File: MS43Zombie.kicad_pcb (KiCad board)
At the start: 2 copper layers, 165 x 119.2 mm, 223 parts, among them IC1 XL1509-5.0E1, IC10 NCV8402ASTT1G, IC11 NCV8402ASTT1G, IC12 TJA1020T_CM,118, IC13 NCV8402ASTT1G, IC14 NCV8402ASTT1G, IC15 NCV8402ASTT1G, IC16 NCV8402ASTT1G, IC17 TJA1055T_3_C,518, IC18 MCP25625T-E_ML, IC19 NCV7356D1R2G, IC2 M24M02-DRMN6TP, IC20 MAX3221ECPWR, IC21 FAN3122TMX, IC22 FAN3122TMX, IC23 FAN3122TMX, IC24 AD5160BRJZ5-R2, IC25 AD5160BRJZ5-R2, IC26 TDA2822D013TR, IC3 NCV8402ASTT1G, IC4 NCV8402ASTT1G, IC5 NCV8402ASTT1G, IC6 NCV8402ASTT1G, IC7 NCV8402ASTT1G, IC8 NCV7356D1R2G, IC9 NUP1105LT1G, J1 7-967288-1, J3 75867-101LF, J4 Conn_01x03, Q1 MMBT3904, Q2 NCV8461DR2G, Q3 MMBT3904, Q4 MMBT3904, Q5 MMBT3904, U1 AMS1117-3.3, U12 SN65HVD230, U16 SN65HVD230, U17 STM32F107VCT6, U19 SN65HVD230, U3 SN65HVD230, U4 SN65HVD230, U8 SN65HVD230, Y1 X50328MSB2GI, Y2 X322516MLB4SI

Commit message: Checkpoint before trying 4 layer
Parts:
- removed C1, C71: 470uF 25V, Capacitor_SMD:CP_Elec_10x10
- removed C11, C2, C37, C38, C39, C40, C41, C5, C52, C57, C70, C73: 0.1uF, Capacitor_SMD:C_0805_2012Metric
- removed C16, C47, C48: 100pF, Capacitor_SMD:C_0805_2012Metric
- removed C18, C20, C22, C26, C42, C43, C49, C51, C59, C60, C61, C7, C72, C76, C77: 1uF, Capacitor_SMD:C_0805_2012Metric
- removed C3: 10uF, Capacitor_SMD:C_0805_2012Metric
- removed C35, C36: 22pF, Capacitor_SMD:C_0805_2012Metric
- removed C45: 10nF, Capacitor_SMD:C_0805_2012Metric
- removed C53, C55, C56: 0.47uF, Capacitor_SMD:C_0805_2012Metric
- removed C6, C8, C9: 100uF 6.3V, Capacitor_Tantalum_SMD:CP_EIA-1608-08_AVX-J
- removed C74, C75: 100uF, Capacitor_Tantalum_SMD:CP_EIA-1608-08_AVX-J
- removed D1, D2: SS54B, SamacSys_Parts:DIOM5336X244N
- removed D10, D12: 1N4148W-7-F, digikey-footprints:SOD-123
- removed D3, D6: LED, LED_SMD:LED_0805_2012Metric
- removed D8: 12V, Diode_SMD:D_SOD-123
- removed FB2: MH2029-300Y, SamacSys_Parts:BEADC2016X130N
- removed IC10, IC11, IC13, IC15, IC16, IC5: NCV8402ASTT1G, SamacSys_Parts:SOT230P700X175-4N
- removed IC17: TJA1055T_3_C,518, SamacSys_Parts:SOIC127P600X175-14N
- removed IC18: MCP25625T-E_ML, SamacSys_Parts:QFN65P600X600X100-29N-D
- removed IC19, IC8: NCV7356D1R2G, SamacSys_Parts:SOIC127P600X175-8N
- removed IC20: MAX3221ECPWR, SamacSys_Parts:SOP65P640X120-16N
- removed IC21, IC22, IC23: FAN3122TMX, SamacSys_Parts:SOIC127P600X175-8N
- removed IC26: TDA2822D013TR, SamacSys_Parts:SOIC127P600X175-8N
- removed IC9: NUP1105LT1G, SamacSys_Parts:SOT96P237X111-3N
- removed JP1, JP10, JP11, JP12, JP13, JP14, JP15, JP2, JP3, JP4, JP5, JP6, JP7, JP8, JP9: SolderJumper_2_Open, Jumper:SolderJumper-2_P1.3mm_Open_Pad1.0x1.5mm
- removed L1: SWRB1207S-680MT, SamacSys_Parts:INDPM125125X800N
- removed R13: 2.7K, Resistor_SMD:R_0805_2012Metric
- removed R14: 6.49k, Resistor_SMD:R_0805_2012Metric
- removed R15: 1k, Resistor_SMD:R_0805_2012Metric
- removed R18, R29: 4K7, Resistor_SMD:R_0805_2012Metric
- removed R19, R30: 1K5, Resistor_SMD:R_0805_2012Metric
- removed R45, R46, R57, R58, R59, R62, R63, R71, R73: 1K, Resistor_SMD:R_0805_2012Metric
- removed R55, R61: 2K7, Resistor_SMD:R_0805_2012Metric
- removed R65: 120R, Resistor_SMD:R_0805_2012Metric
- removed R66, R67: 4R7, Resistor_SMD:R_0805_2012Metric
- removed R69, R70: 10K, Resistor_SMD:R_0805_2012Metric
- removed U1: AMS1117-3.3, Package_TO_SOT_SMD:SOT-223-3_TabPin2
- removed U17: STM32F107VCT6, Package_QFP:LQFP-100_14x14mm_P0.5mm
- removed Y1: X50328MSB2GI, SamacSys_Parts:RESC5032X135N
- removed Y2: X322516MLB4SI, SamacSys_Parts:X322516MLB4SI
- added IC27: NCV8402ASTT1G, SamacSys_Parts:SOT230P700X175-4N, F.Cu at (117.4, 65.2)
- added J2: EXT1, Connector_PinHeader_2.54mm:PinHeader_2x20_P2.54mm_Vertical, B.Cu at (164.4, 131.3)
- added Q6: NCV8461DR2G, SamacSys_Parts:SOIC127P600X175-8N, F.Cu at (211.4, 65.2)
- added Q7: MMBT3904, Package_TO_SOT_SMD:SOT-23, F.Cu at (203.8, 75.4)
- C4: value 0.1uF -> 1uF
- IC1: value XL1509-5.0E1 -> NCV8402ASTT1G; footprint SamacSys_Parts:SOIC127P600X175-8N -> SamacSys_Parts:SOT230P700X175-4N
- IC12: footprint SamacSys_Parts:SOIC127P600X175-8N -> Package_SO:SO-8_3.9x4.9mm_P1.27mm
- IC24, IC25: footprint SamacSys_Parts:SOT65P280X145-8N -> Package_TO_SOT_SMD:SOT-23-8
- J4: value Conn_01x03 -> EXT2; footprint Connector_PinHeader_1.00mm:PinHeader_1x03_P1.00mm_Vertical -> Connector_PinHeader_2.54mm:PinHeader_2x20_P2.54mm_Vertical; moved to B.Cu
- R11: value 200R -> 1K
- R33: value 680R -> 4K7
- R34: value 10K -> 1K5
- R4: value 470R -> 1K
- moved FL16 270.8 mm to (184.7, 77.9), turned to 270 degrees
- moved R72 267.8 mm to (186.0, 81.7), turned to 90 degrees
- moved R76 265.5 mm to (183.5, 81.7), turned to 90 degrees
- moved C62 263.2 mm to (180.9, 81.7), turned to 90 degrees
- moved FL12 262.2 mm to (175.8, 77.9), turned to 270 degrees
- moved R64 259.4 mm to (177.1, 81.7), turned to 90 degrees
- moved R68 257.0 mm to (174.6, 81.7), turned to 90 degrees
- moved C58 254.6 mm to (172.0, 81.7), turned to 90 degrees
- moved R2 207.0 mm to (210.5, 87.1), turned to 0 degrees
- moved Q4 205.8 mm to (206.0, 85.0)
- moved R1 200.5 mm to (210.5, 84.2), turned to 0 degrees
- moved R11 198.7 mm to (208.2, 77.5), turned to 0 degrees
- moved C17 187.4 mm to (111.4, 75.4)
- moved D11 187.4 mm to (112.3, 80.5)
- moved D13 187.4 mm to (107.3, 74.1)
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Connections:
- net /CAN_EXT2H renamed /CAN_EXT2+
- net /CAN_EXT2L renamed /CAN_EXT2-
- net /GroundElectricThrottleBody renamed /OIL_PUMP_POWER
- net /GroundExhaustCamshaftSensor renamed /MG2_TEMP-
- net /GroundIntakeCamshaft renamed /MG1_TEMP+
- net /GroundMAF renamed /MG1_TEMP-
- net /Heater Control/HeaterPumpPWMPin renamed /COOLANT_PUMP_1
- net /PWM02SensorHeaterPostCatBank2 renamed /HeaterPumpPWM
- net /SignalO2SensorPostCatBank2 renamed /HeaterPumpEnable
- net Net-(J1-PadD1) renamed /SignalShiftLock
- net Net-(J1-PadD2) renamed /SupplyShiftLock
- C4 pad 1: GND -> /12V_MEASURE
- C4 pad 2: /3_3Vcc -> GND
- IC1 pad 1: /12Vcc -> /ReverseRelayDRV
- IC1 pad 3: /5Vcc -> GND
- IC1 pad 4: GND -> /ReverseLightRelay
- IC14 pad 1: /GP1_DRV -> /FuelPumpRelayDRV
- IC14 pad 4: /GP_OUT1 -> /SignalFuelPumpRelay
- IC6 pad 4: /SignalElectricThrottleBodyPot2 -> /TRANS_SL1-
- J1 pad A7: /+12Vin -> /A2076
- J1 pad B14: /GP_OUT1 -> /InverterCoolingPumpSignal
- J1 pad B22: GND -> /GroundO2SensorPostCatBank1
- J1 pad B6: /DataLinkMFW -> /GearboxDiagnosticLink
- J1 pad B8: Net-(J1-PadB8) -> /ReverseLightRelay
- J1 pad C1: /REQ+ -> /PWMCoolantPump1
- J1 pad C10: /SignalElectricThrottleBodyPot2 -> Net-(J1-PadC10)
- J1 pad C11: /TRANS_SP -> Net-(J1-PadC11)
- J1 pad C2: /REQ- -> /PWMCoolantPump2
- J1 pad C21: /FORWARD -> /GroundCrankshaft
- J1 pad C22: /REVERSE -> /SignalIAT
- J1 pad C26: /POT1_OUT -> Net-(J1-PadC26)
- J1 pad C27: /POT2_OUT -> /SignalEngineOilTemp
- J1 pad C3: /HTM+ -> Net-(J1-PadC3)
- J1 pad C37: /GP_OUT2 -> /SignalFI5
- J1 pad C39: /RS232_TX -> Net-(J1-PadC39)
- J1 pad C4: /HTM- -> Net-(J1-PadC4)
- J1 pad C40: /RS232_RX -> /REQ-
- J1 pad C41: /CAN3_EXTH -> /REQ+
- J1 pad C42: /CAN3_EXTL -> /HTM-
- J1 pad C43: /ElectricThrottleBodyActuator1 -> /HTM+
- J1 pad C44: /ElectricThrottleBodyActuator2 -> /MTH-
- J1 pad C45: /CharacteristicMapCoolingThermostat -> /MTH+
- J1 pad C46: /IdleSpeedActuatorClosing -> /CLK-
- J1 pad C47: /IdleSpeedActuatorOpening -> /CLK+
- J1 pad C48: /ShieldKnockSensors -> /TRANS_SL2-
- J1 pad C49: /VariableIntakeManifoldFlap -> /TRANS_SL1-
- J1 pad C5: /MTH+ -> /SignalIntakeCamshaft
- J1 pad C50: Net-(J1-PadC50) -> /TRANS_SP
- J1 pad C51: Net-(J1-PadC51) -> /POT2_OUT
- J1 pad C52: /SignalSecondaryAirPumpValve -> /POT1_OUT
- J1 pad C6: /MTH- -> Net-(J1-PadC6)
- J1 pad C7: /CLK+ -> /SupplyElectricThrottleBody
- J1 pad C8: /CLK- -> /SignalCrankshaftSensor
- J1 pad C9: /TRANS_SL2- -> Net-(J1-PadC9)
- J1 pad D29: /GP_OUT3 -> /SignalACCompressorRelay
- J1 pad D32: /DataLinkMFW -> /EngineDiagnosticLinkTXD
- J1 pad D36: /CAN+ -> /CAN-
- J1 pad D37: /CAN- -> /CAN+
- J1 pad D5: Net-(J1-PadD5) -> /FORWARD
- J1 pad D6: Net-(J1-PadD6) -> /REVERSE
- J4 pad 1: Net-(J4-Pad1) -> /3_3Vcc
- J4 pad 2: GND -> /3_3Vcc
- J4 pad 3: Net-(J4-Pad3) -> /RESET
- Q4 pad 3: /Heater Control/HeaterPumpPWMOutput -> /PWMCoolantPump1
- R11 pad 1: /HeaterNTCSignal -> /12Vcc
- R11 pad 2: GND -> /PWMCoolantPump2
- R2 pad 2: /Heater Control/HeaterPumpPWMOutput -> /PWMCoolantPump1
- R23 pad 1: Net-(R23-Pad1) -> /3_3Vcc
- R27 pad 1: Net-(R23-Pad1) -> /3_3Vcc
- R3 pad 2: /GroundIAT -> /EWS
- R33 pad 1: Net-(R33-Pad1) -> /12V_MEASURE
- R33 pad 2: Net-(D6-Pad2) -> /12Vcc
- R34 pad 1: GND -> /12V_MEASURE
- R34 pad 2: Net-(R34-Pad2) -> GND
- R4 pad 1: /3_3Vcc -> Net-(Q7-Pad1)
- R4 pad 2: Net-(D3-Pad2) -> /COOLANT_PUMP_2
- R42 pad 2: /ANALOG1_IN -> /CoolantTempIn
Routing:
- net /3_3Vcc: track 20.8 -> 155.4 mm, vias 0 -> 10
- net /5Vcc: track 56.3 -> 0.00 mm, vias 7 -> 0
- net /PC1: track 0.00 -> 50.6 mm, vias 0 -> 1
- net /PC0: track 0.00 -> 49.0 mm, vias 0 -> 1
- net /PedalSignal2: track 0.00 -> 47.9 mm, vias 0 -> 1
- net /PedalSignal1: track 0.00 -> 27.8 mm
- net /CAN_EXT2+: track 0.00 -> 26.0 mm, vias 0 -> 1
- net /TRANS_SL1-: track 0.00 -> 25.4 mm
- net /CAN_EXT2-: track 0.00 -> 24.3 mm, vias 0 -> 1
- net /FOR_IN: track 0.00 -> 23.7 mm
- net /TRANS_SL2-: track 0.00 -> 23.0 mm
- net /SignalFuelPumpRelay: track 0.00 -> 22.2 mm, vias 0 -> 1
- net /ReverseLightRelay: track 0.00 -> 20.9 mm, vias 0 -> 1
- net /+12Vin: track 19.7 -> 0.00 mm
- net /FuelInjectorRelay: track 0.00 -> 18.4 mm
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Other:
- board text added: "DME Harness"
- board text added: "Inverter"
- board text added: "Power"
- board text added: "Transmission"
- board text added: "Vehicle"

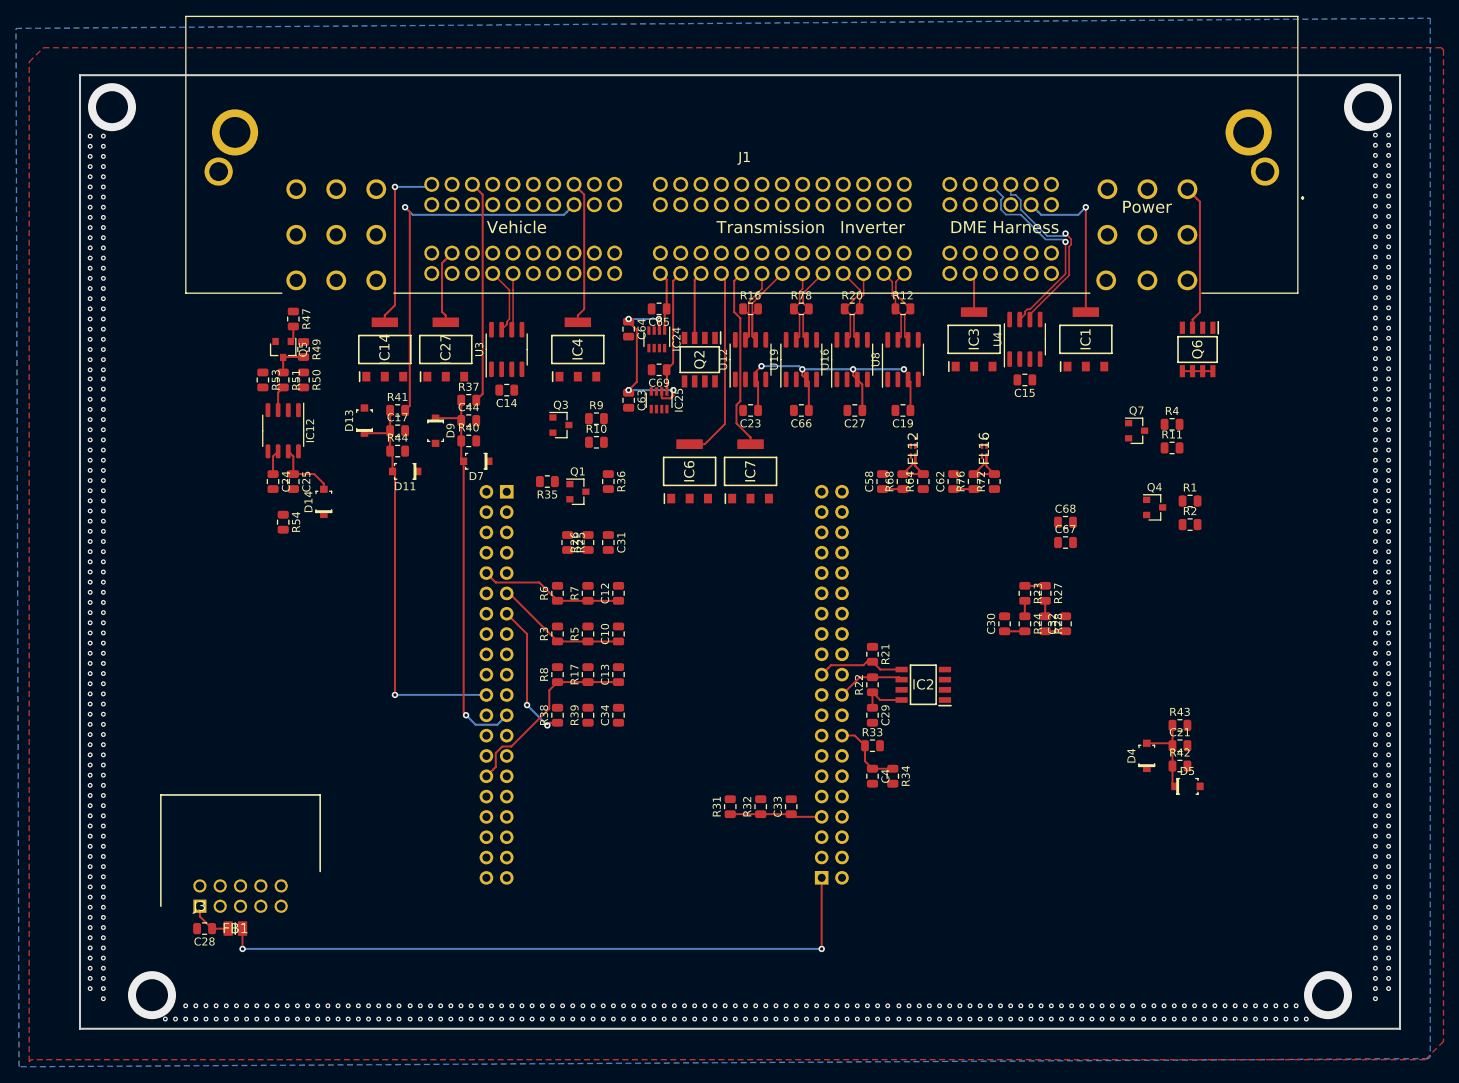
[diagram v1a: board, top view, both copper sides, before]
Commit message: 4 layer board that passes checks
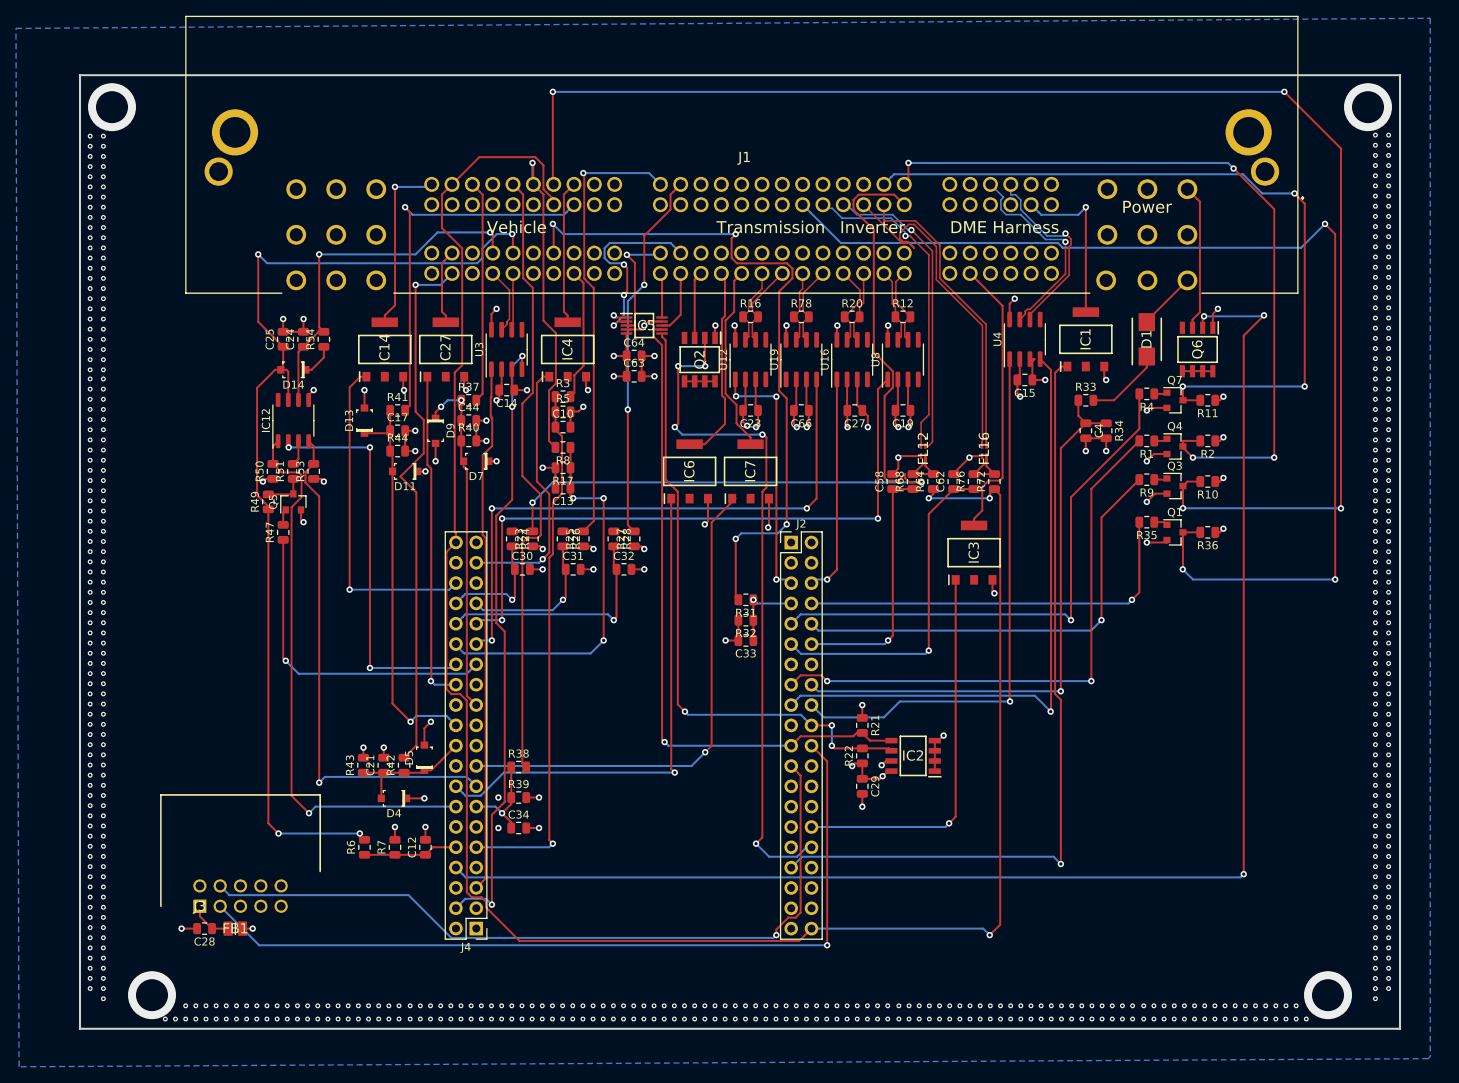
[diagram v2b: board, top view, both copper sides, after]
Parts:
- removed C65, C68, C69: 0.1uF, Capacitor_SMD:C_0805_2012Metric
- removed C67: 10uF, Capacitor_SMD:C_0805_2012Metric
- removed IC24, IC25: AD5160BRJZ5-R2, Package_TO_SOT_SMD:SOT-23-8
- added D1: SS54B, SamacSys_Parts:DIOM5336X244N, F.Cu at (205.1, 64.0)
- added IC5: AD5243BRMZ2.5, SamacSys_Parts:SOP50P490X110-10N, F.Cu at (142.2, 62.2)
- J2, J4: moved to F.Cu
- moved R43 102.2 mm to (107.1, 117.2), turned to 90 degrees
- moved C21 99.6 mm to (109.7, 117.2), turned to 90 degrees
- moved R42 97.0 mm to (112.2, 117.2), turned to 90 degrees
- moved D5 95.4 mm to (114.8, 116.3), turned to 90 degrees
- moved D4 94.3 mm to (110.9, 121.3), turned to 180 degrees
- moved Q3 77.1 mm to (208.6, 82.3)
- moved R10 76.6 mm to (212.7, 81.7), turned to 180 degrees
- moved R36 75.2 mm to (212.7, 88.1), turned to 180 degrees
- moved R35 75.1 mm to (205.1, 86.8)
- moved Q1 74.8 mm to (208.6, 88.1)
- moved R9 69.2 mm to (205.1, 81.5), turned to 180 degrees
- moved R24 65.0 mm to (125.7, 88.9)
- moved R23 61.9 mm to (128.3, 88.9), turned to 90 degrees
- moved C30 60.7 mm to (127.0, 92.7), turned to 0 degrees
- moved C32 55.6 mm to (139.7, 92.7), turned to 0 degrees
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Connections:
- net /USART1_RX renamed /PC11
- net /USART1_TX renamed /PC10
- C10 pad 1: /START_IN -> /PD5
- C21 pad 1: /PC2 -> /CoolantTempIn
- C25 pad 1: /12Vcc -> /IGNITION_T15
- C58 pad 1: /PC5 -> /MG1_TEMP_IN
- C62 pad 1: /PC4 -> /MG2_TEMP_IN
- D14 pad A: /12Vcc -> /IGNITION_T15
- D4 pad A: /PC2 -> /CoolantTempIn
- D5 pad K: /PC2 -> /CoolantTempIn
- IC1 pad 1: /ReverseRelayDRV -> /PD13
- IC12 pad 7: /12Vcc -> /IGNITION_T15
- IC27 pad 1: /PE12 -> /ACCompressorRelayDRV
- J1 pad C15: /MG2_TEMP- -> /MG2_TEMP+
- J1 pad C16: /MG2_TEMP+ -> /MG2_TEMP-
- J1 pad C17: /MG1_TEMP- -> /MG1_TEMP+
- J1 pad C18: /MG1_TEMP+ -> /MG1_TEMP-
- J1 pad C20: /OIL_PUMP_POWER -> Net-(J1-PadC20)
- J1 pad C38: /SignalFI6 -> /DigitalPotA1
- J1 pad C39: Net-(J1-PadC39) -> /DigitalPotW2
- J1 pad C51: /POT2_OUT -> /DigitalPotA2
- J1 pad C52: /POT1_OUT -> /DigitalPotW1
- J1 pad D38: /CoolantOutletTempGround -> GND
- J2 pad 10: /PE11 -> /ELECTRIC_FAN
- J2 pad 11: /PE12 -> /MG2_TEMP_IN
- J2 pad 12: /PE13 -> /MG1_TEMP_IN
- J2 pad 15: /PB0 -> /COOLANT_PUMP_1
- J2 pad 30: /LIN_WAKE -> /INV_POWER
- J2 pad 31: /LIN_NSLP -> /PD11
- J2 pad 9: /PE10 -> /COOLANT_PUMP_2
- J4 pad 11: /START_IN -> /USB_VBUS_ON
- J4 pad 20: /PC3 -> /CoolantTempIn
- J4 pad 24: /INV_POWER -> Net-(J4-Pad24)
- J4 pad 26: /PA6 -> /ACCompressorRelayDRV
- J4 pad 27: /PA5 -> /LIN_WAKE
- J4 pad 28: /PA4 -> /LIN_NSLP
- J4 pad 36: /PE1 -> /FuelPumpRelayDRV
- J4 pad 37: /PE0 -> /OIL_POWER
- J4 pad 6: /POT2_CS -> Net-(J4-Pad6)
- J4 pad 7: /POT1_CS -> Net-(J4-Pad7)
- J4 pad 8: /PD4 -> /FuelInjectorDRV
- Q6 pad 2: /FuelInjectorRelay/SP -> /FuelInjectorDRV
- R10 pad 1: /12Vcc -> /A8680
- R11 pad 1: /12Vcc -> /A8680
- R2 pad 1: /12Vcc -> /A8680
- R3 pad 1: /START_IN -> /PD5
- R36 pad 1: /12Vcc -> /A8680
- R42 pad 1: /PC2 -> /CoolantTempIn
- R42 pad 2: /CoolantTempIn -> /CoolantOutputTempSignal
- R43 pad 1: /PC2 -> /CoolantTempIn
- R49 pad 1: /12Vcc -> /IGNITION_T15
- R5 pad 1: /START_IN -> /PD5
- R68 pad 1: /PC5 -> /MG1_TEMP_IN
- R76 pad 1: /PC4 -> /MG2_TEMP_IN
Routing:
- net /5Vcc: track 0.00 -> 247.7 mm, vias 0 -> 3
- net /PWMElectricFan: track 0.00 -> 183.0 mm, vias 0 -> 4
- net /FuelInjectorDRV: track 0.00 -> 179.1 mm, vias 0 -> 3
- net GND: track 0.00 -> 168.7 mm, vias 567 -> 629
- net /OIL_PUMP_PWM: track 0.00 -> 140.1 mm, vias 0 -> 3
- net /IGNITION_T15: track 0.00 -> 129.2 mm, vias 0 -> 4
- net /TRANS_PB1: track 1.94 -> 106.0 mm, vias 0 -> 2
- net /UART3_TX: track 0.00 -> 103.6 mm, vias 0 -> 1
- net /PD13: track 0.00 -> 98.2 mm, vias 0 -> 1
- net /PWMCoolantPump1: track 0.00 -> 97.0 mm, vias 0 -> 4
- net /PWMCoolantPump2: track 0.00 -> 96.6 mm, vias 0 -> 3
- net /UART3_RX: track 0.00 -> 95.8 mm, vias 0 -> 1
- net /3_3Vcc: track 155.4 -> 64.3 mm, vias 10 -> 20
- net /SignalBrakeLightSwitch: track 0.00 -> 86.4 mm, vias 0 -> 4
- net /SP: track 0.00 -> 86.1 mm, vias 0 -> 5
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- added copper zone on In2.Cu, net /3_3Vcc
- added copper zone on In2.Cu, net /A8680
- added copper zone on In1.Cu, net GND
- removed copper zone on F.Cu, net GND
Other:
- copper layers 2 -> 4
